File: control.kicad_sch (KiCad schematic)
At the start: 67 parts, among them J2 OUTPUT, J3 OLED 0.96in I2C, J4 SWD + UART, Q5 TIP127, SW1 EC11, SW2 OUTPUT, SW3 SELECT, SW4 BACK, U10 STM32G030C8T6, U8 LM358, U9 INA181A2

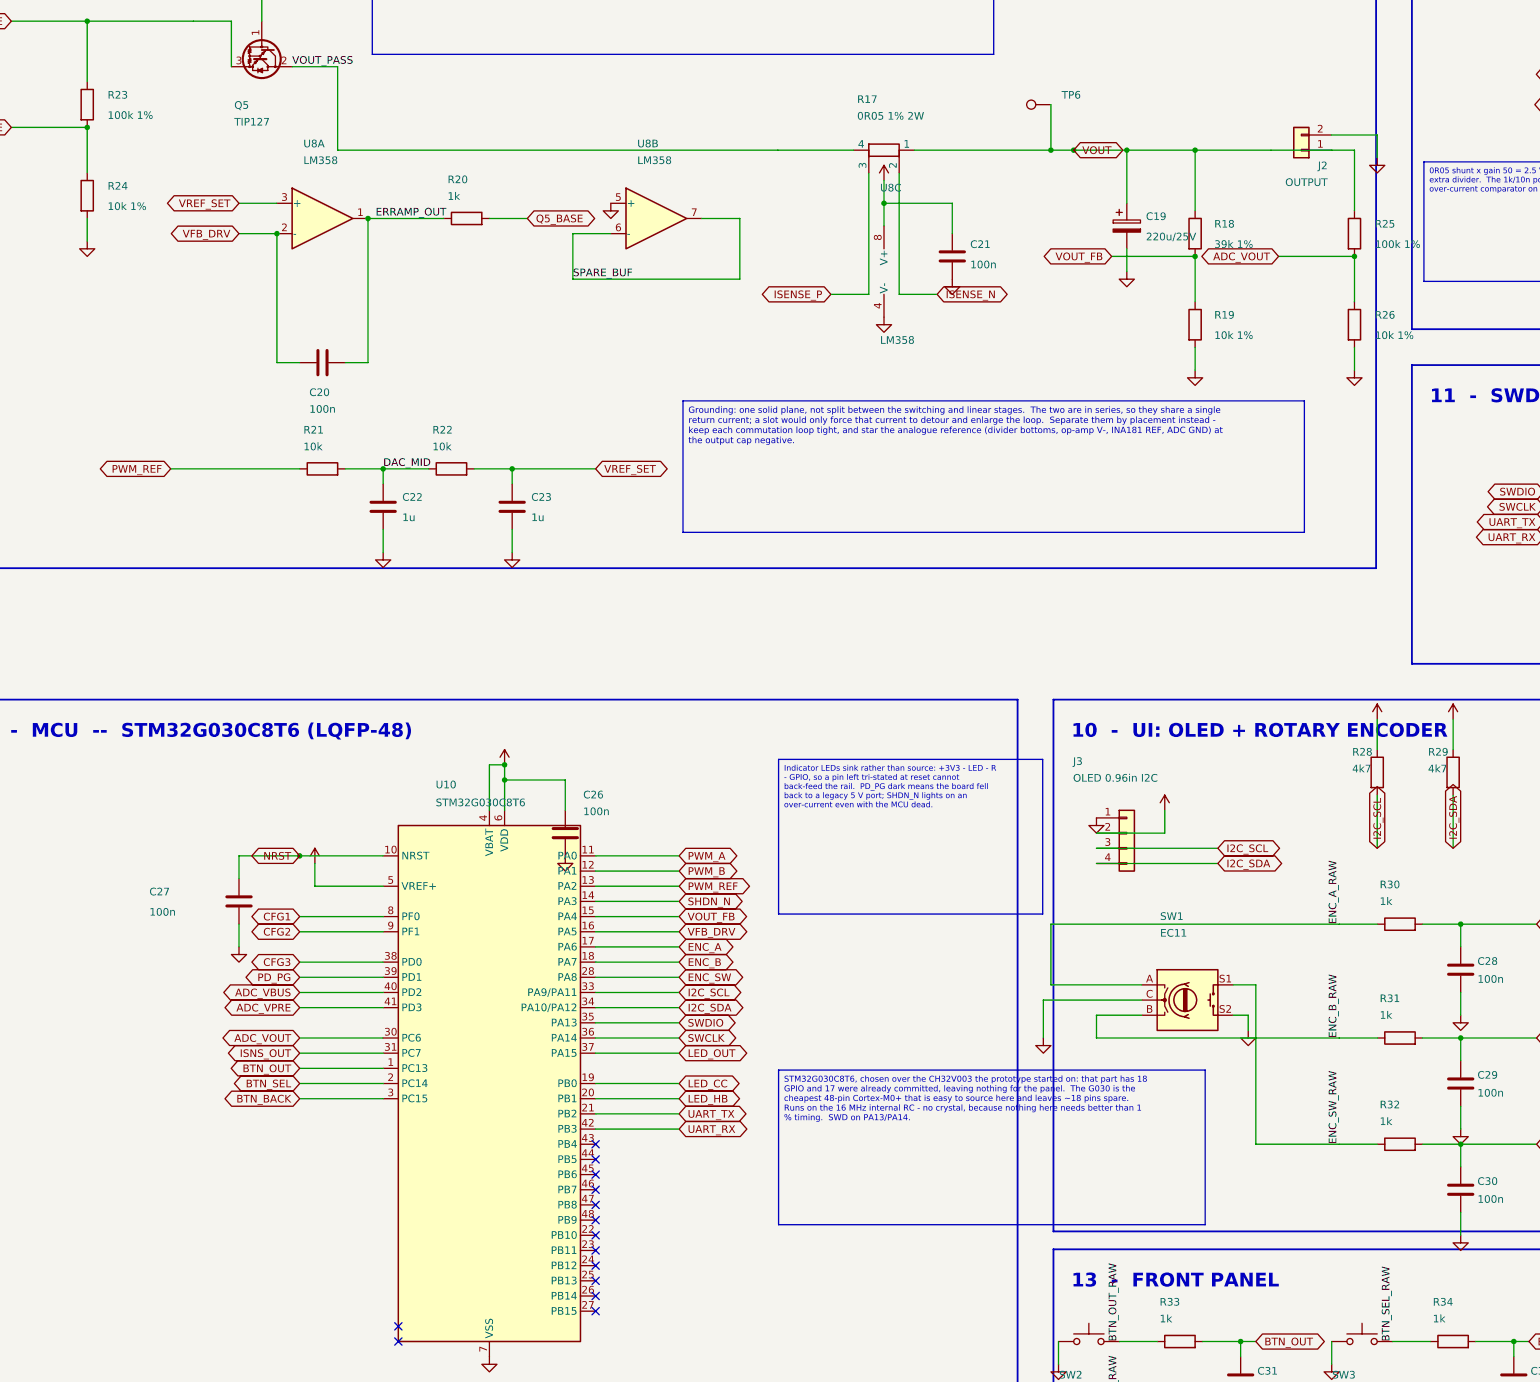
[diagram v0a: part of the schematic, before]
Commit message: v1.2: 0-36 V range, and analogue nets onto real ADC pins
Two changes, one of them serious.

The serious one: ADC_VBUS, ADC_VPRE, ADC_VOUT and ISNS_OUT were on PD2, PD3,
PC6 and PC7.  None of those four pins has an ADC channel on this part, so not
one of the four measurements could ever have been taken.  They move to PA0,
PA1, PA4 and PA5 - ADC_IN0, 1, 4 and 5 - and the timer outputs shuffle to
suit.

The range change: the feedback divider goes from 39k/10k to 150k/10k, which
puts 36 V at the top of the range instead of 20 V, and the divider ratio
becomes exactly 16:1 so the reference maths stays integer.  The pre-regulator
bulk capacitor and the output capacitor go to 63 V parts to match, and the
monitor dividers are rescaled the same way.
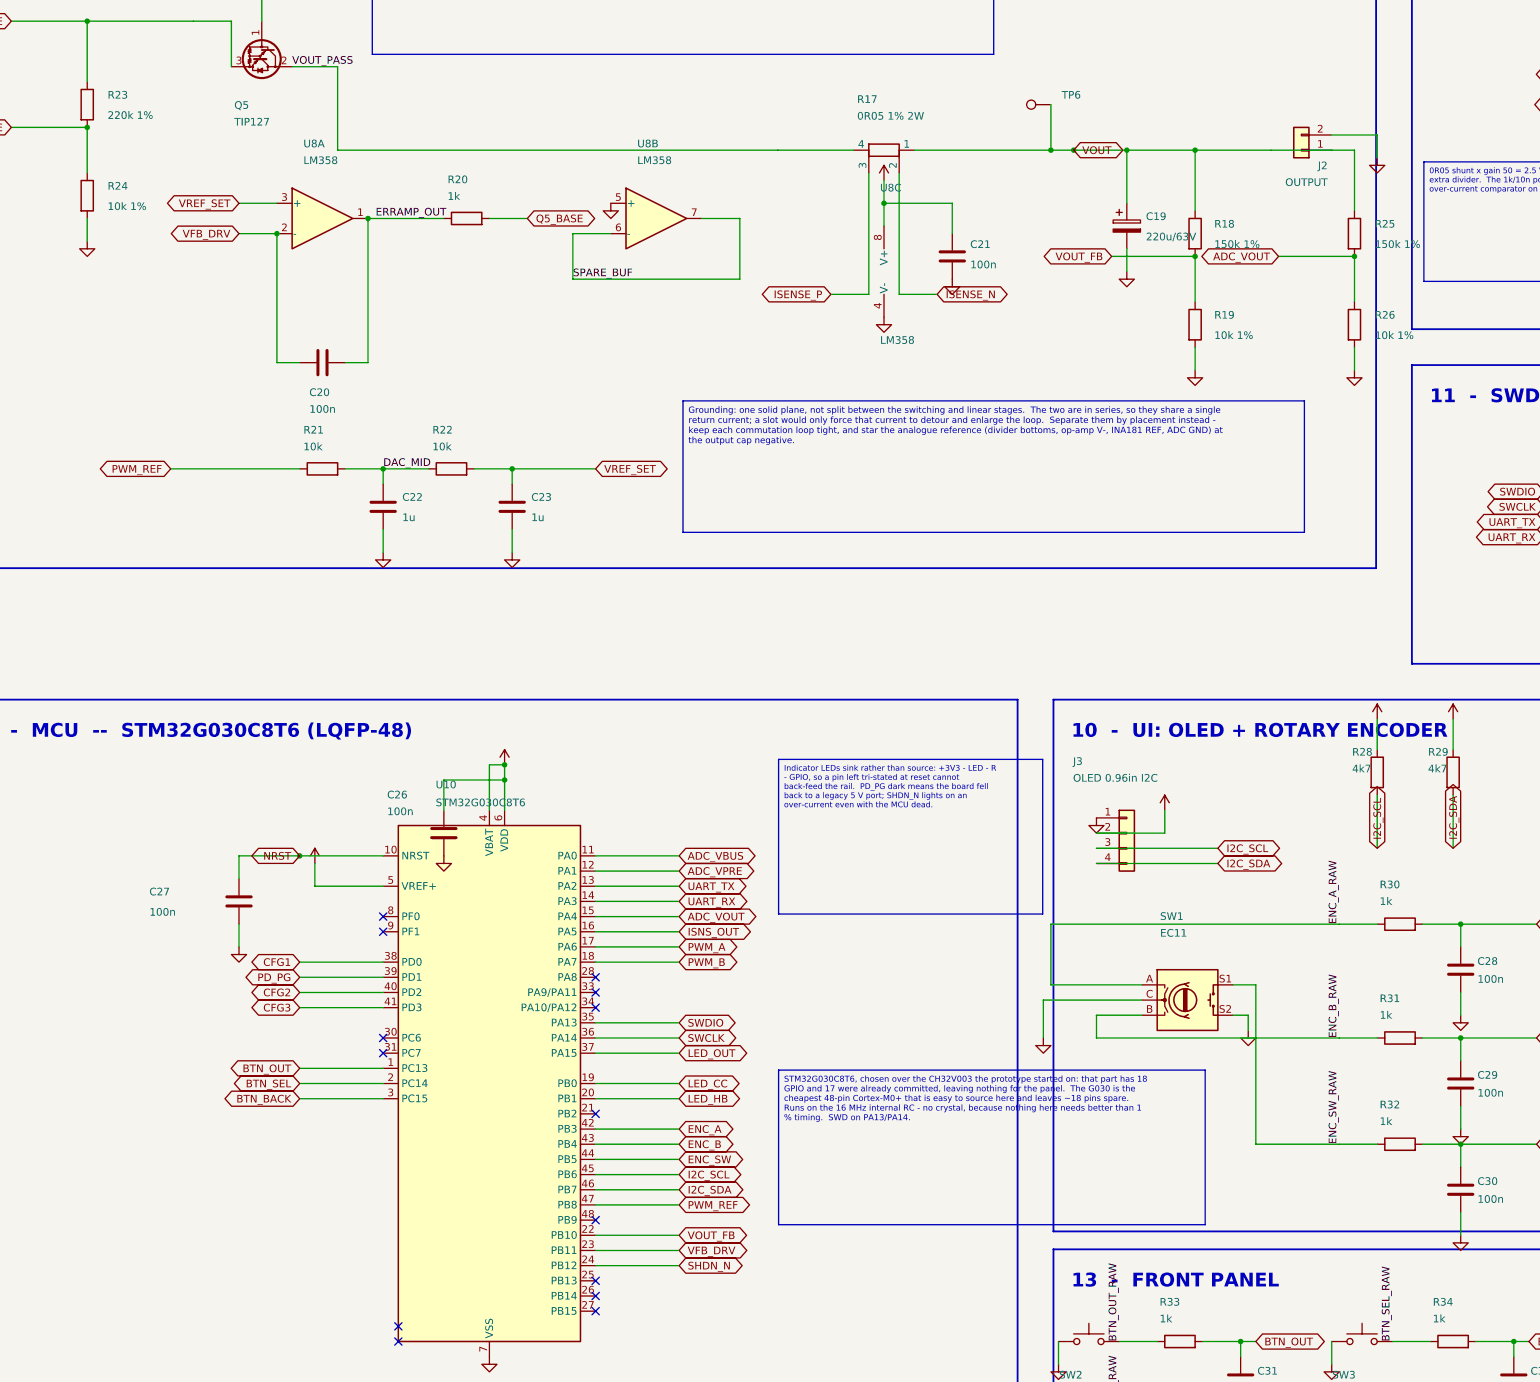
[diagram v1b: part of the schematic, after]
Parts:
- C19: value 220u/25V -> 220u/63V
- R18: value 39k 1% -> 150k 1%
- R23: value 100k 1% -> 220k 1%
- R25: value 100k 1% -> 150k 1%
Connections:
- net ADC_VBUS: now also U10.11 (PA0); no longer U10.40 (PD2)
- net ADC_VOUT: now also U10.15 (PA4); no longer U10.30 (PC6)
- net ADC_VPRE: now also U10.12 (PA1); no longer U10.41 (PD3)
- net CFG1: now also U10.38 (PD0); no longer U10.8 (PF0)
- net CFG2: now also U10.40 (PD2); no longer U10.9 (PF1)
- net CFG3: now also U10.41 (PD3); no longer U10.38 (PD0)
- net ENC_A: now also U10.42 (PB3); no longer U10.17 (PA6)
- net ENC_B: now also U10.43 (PB4); no longer U10.18 (PA7)
- net ENC_SW: now also U10.44 (PB5); no longer U10.28 (PA8)
- net I2C_SCL: now also U10.45 (PB6); no longer U10.33 (PA9/PA11)
- net I2C_SDA: now also U10.46 (PB7); no longer U10.34 (PA10/PA12)
- net ISNS_OUT: now also U10.16 (PA5); no longer U10.31 (PC7)
- net PWM_A: now also U10.17 (PA6); no longer U10.11 (PA0)
- net PWM_B: now also U10.18 (PA7); no longer U10.12 (PA1)
- net PWM_REF: now also U10.47 (PB8); no longer U10.13 (PA2)
- net SHDN_N: now also U10.24 (PB12); no longer U10.14 (PA3)
- net UART_RX: now also U10.14 (PA3); no longer U10.42 (PB3)
- net UART_TX: now also U10.13 (PA2); no longer U10.21 (PB2)
- net VFB_DRV: now also U10.23 (PB11); no longer U10.16 (PA5)
- net VOUT_FB: now also U10.22 (PB10); no longer U10.15 (PA4)

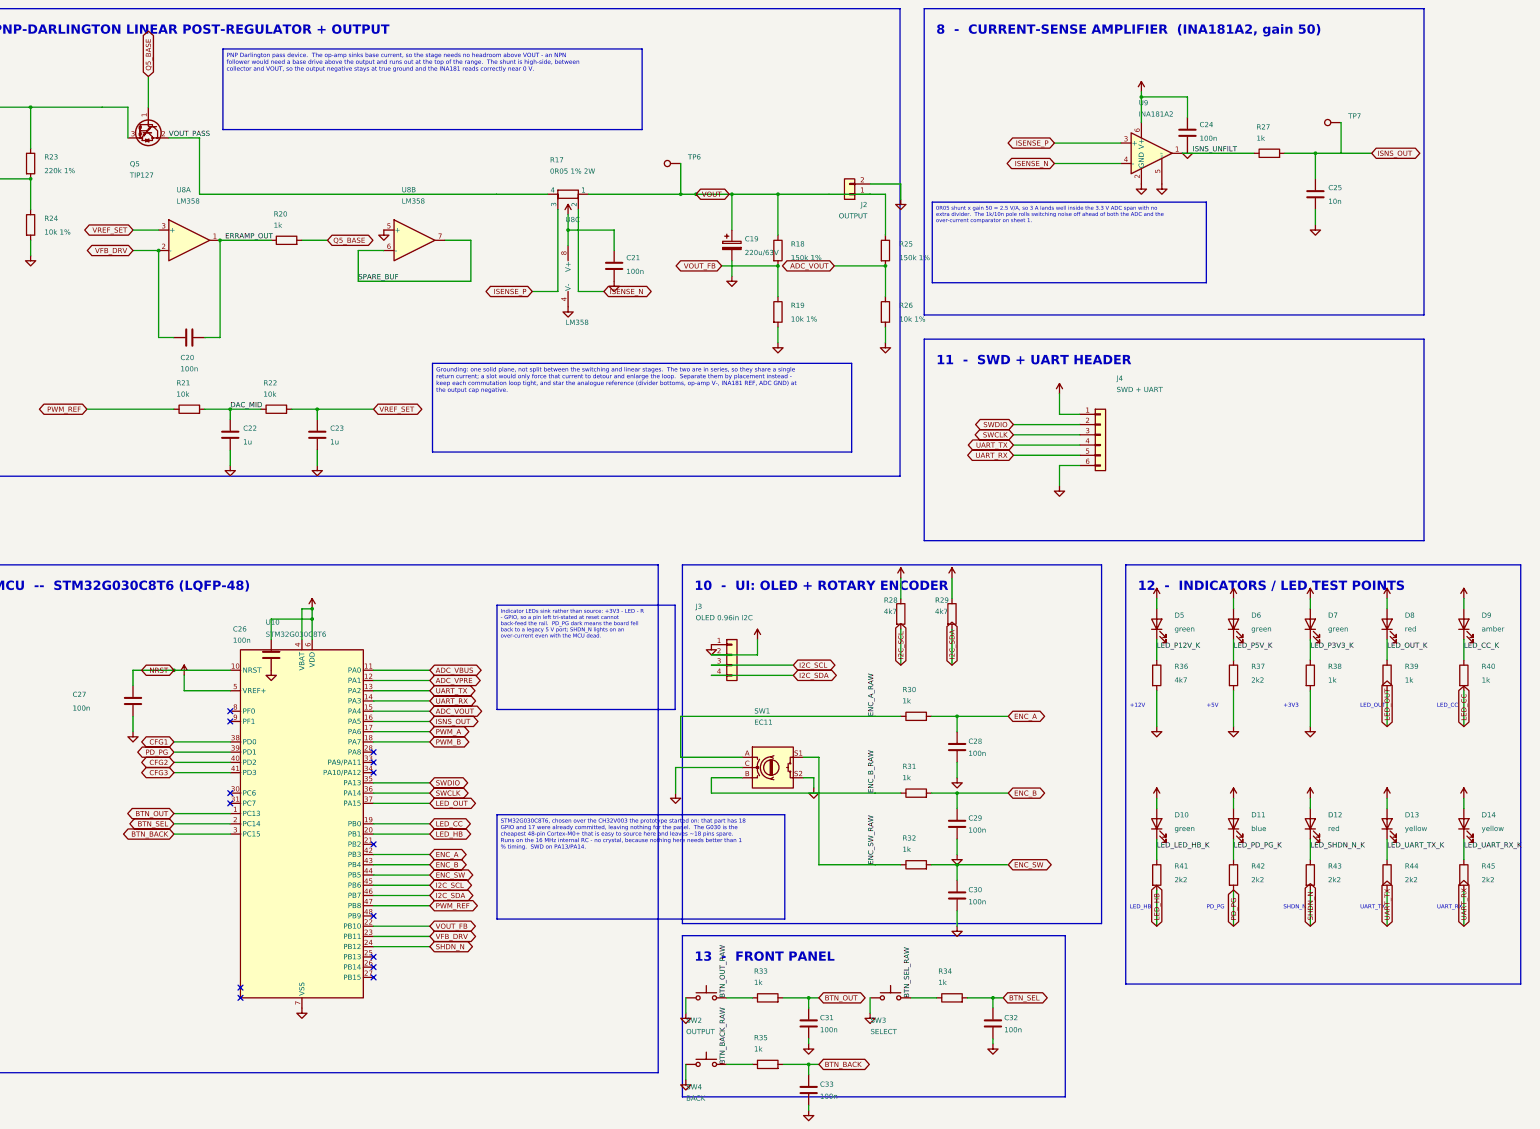
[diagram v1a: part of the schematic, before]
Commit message: v1.3: close the feedback loop, tie the driver returns, rescale the sense chain
Three faults, each of which on its own would have stopped the board working.
All three came out of reading the exported netlist rather than the schematic.

The feedback loop was never closed.  The output divider tap and the error
amplifier's inverting input were two separate nets: the divider went only to an
MCU analogue input, and the amplifier input saw only its compensation
capacitor.  With no DC path around it the amplifier is a bare integrator - its
input floats on bias current and its output ramps to a rail - so the pass
device would have sat hard on or hard off.  The output would not have
regulated; it would have latched.  Both now carry one name and are one node,
which gives V_OUT = 16 x V_REF, exactly what set_ref_dac() already assumes.

The high-side driver returns were open.  Each IRS2104's VS pin sat on a net of
its own instead of on the switch node it references.  VS is what the bootstrap
capacitor and the high-side output float on, so with it open the capacitor
cannot refresh and neither high-side FET switches at all.  Both now tie to the
power switch node.

The current sense saturated at 1.32 A.  0.05 ohm into a gain of 50 is 2.5 V/A,
which reaches the 3.3 V ADC ceiling well below the 3 A the shunt and the pass
device are rated for.  Above that the reading sticks, so the current limit, the
constant-current indicator and the adaptive headroom all stop responding while
the analogue loop carries on delivering current.  0.01 ohm into a gain of 100
gives 1 V/A: full scale 3.3 A, and a fifth of the dissipation in the shunt.

That last change also makes the over-current trip reachable.  At 2.5 V/A a
3.2 A threshold needed 8 V of reference, which the 5 V rail cannot produce, so
the divider had been set to whatever fitted and tripped at 0.64 A.  At 1 V/A
the same threshold needs 3.2 V, and 22k over 39k puts it there.

ERC is clean apart from the library-symbol mismatches that come f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
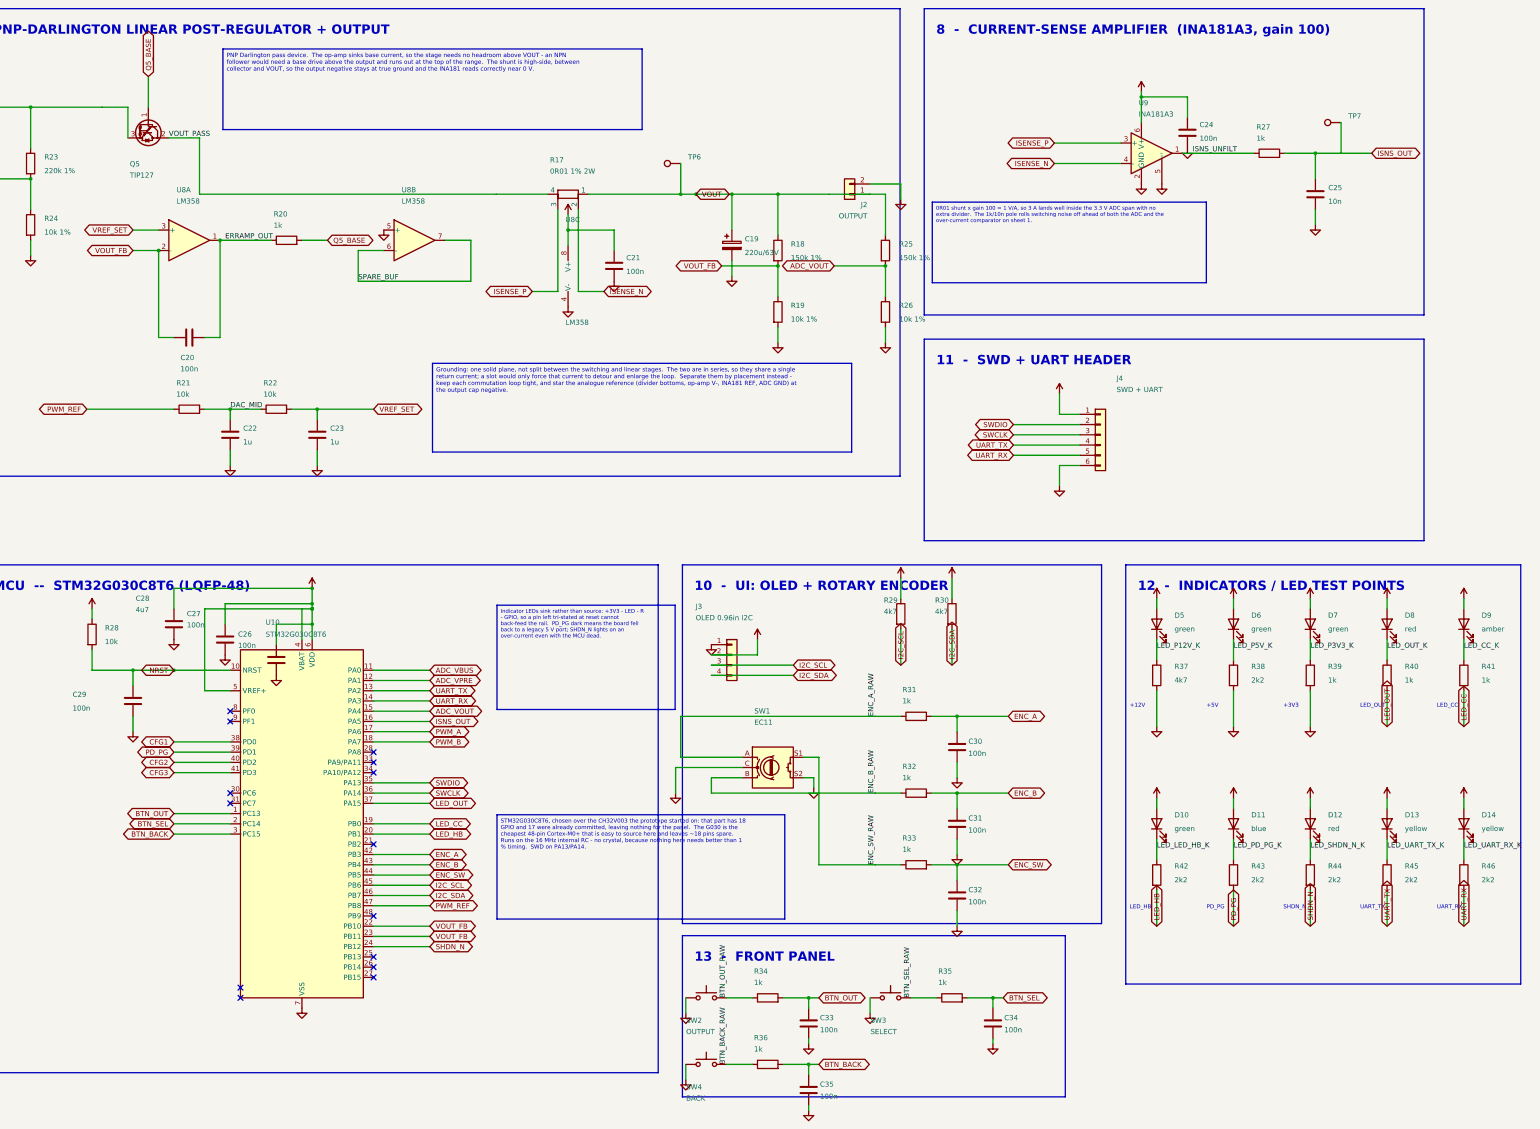
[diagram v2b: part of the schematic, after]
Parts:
- added C34, C35: 100n, Capacitor_SMD:C_0805_2012Metric, symbol Device:C
- added R46: 2k2, Resistor_SMD:R_0805_2012Metric, symbol Device:R
- C28: value 100n -> 4u7
- R17: value 0R05 1% 2W -> 0R01 1% 2W
- R28: value 4k7 -> 10k
- R30: value 1k -> 4k7
- R36: value 4k7 -> 1k
- R37: value 2k2 -> 4k7
- R38: value 1k -> 2k2
- R41: value 2k2 -> 1k
- U9: value INA181A2 -> INA181A3
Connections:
- net VFB_DRV is gone; now on net VOUT_FB: C20.1, U10.23 (PB11), U8.2 (-)
- net +3V3: now also C27.1, C28.1, R30.1
- net BTN_BACK: now also R36.2, C35.1; no longer C33.1, R35.2
- net BTN_BACK_RAW: now also R36.1; no longer R35.1
- net BTN_OUT: now also C33.1, R34.2; no longer C31.1, R33.2
- net BTN_OUT_RAW: now also R34.1; no longer R33.1
- net BTN_SEL: now also R35.2, C34.1; no longer C32.1, R34.2
- net BTN_SEL_RAW: now also R35.1; no longer R34.1
- net ENC_A: now also C30.1, R31.2; no longer C28.1, R30.2
- net ENC_A_RAW: now also R31.1; no longer R30.1
- net ENC_B: now also C31.1, R32.2; no longer C29.1, R31.2
- net ENC_B_RAW: now also R32.1; no longer R31.1
- net ENC_SW: now also C32.1, R33.2; no longer C30.1, R32.2
- net ENC_SW_RAW: now also R33.1; no longer R32.1
- net GND: now also R39.2, C34.2, C35.2; no longer R36.2
- net I2C_SCL: now also R29.2; no longer R28.2
- net I2C_SDA: now also R30.2; no longer R29.2
- net LED_CC: now also R41.2; no longer R40.2
- net LED_CC_K: now also R41.1; no longer R40.1
- net LED_HB: now also R42.2; no longer R41.2
- net LED_LED_HB_K: now also R42.1; no longer R41.1
- net LED_OUT: now also R40.2; no longer R39.2
- net LED_OUT_K: now also R40.1; no longer R39.1
- net LED_P12V_K: now also R37.1; no longer R36.1
- net LED_P3V3_K: now also R39.1; no longer R38.1
- net LED_P5V_K: now also R38.1; no longer R37.1
- net LED_PD_PG_K: now also R43.1; no longer R42.1
- net LED_SHDN_N_K: now also R44.1; no longer R43.1
- net LED_UART_RX_K: now also R46.1; no longer R45.1
- net LED_UART_TX_K: now also R45.1; no longer R44.1
- net NRST: now also C29.1, R28.2; no longer C27.1
- net PD_PG: now also R43.2; no longer R42.2
- net SHDN_N: now also R44.2; no longer R43.2
- net UART_RX: now also R46.2; no longer R45.2
- net UART_TX: now also R45.2; no longer R44.2
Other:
- note added: "8 - CURRENT-SENSE AMPLIFIER (INA181A3, gain 100)"
- note removed: "8 - CURRENT-SENSE AMPLIFIER (INA181A2, gain 50)"
